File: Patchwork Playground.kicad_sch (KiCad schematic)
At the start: 93 parts, among them J1 PADS, J2 USB_C_Receptacle_USB2.0, J3 PADS, J4 POGO, J5 PADS, J6 JST-GH-4P, SW1 SW_SPDT, SW2 SW_SPDT, SW3 SW_SPDT, SW4 BUTTON, SW5 SW_SPDT, SW6 SW_SPDT, SW7 SW_SPDT, U1 SMF05CT1G, U2 M3406, U3 BQ21040DBVR, U4 SMF05CT1G, U5 QMC5883L, U6 BC805M, U7 LSM6DSV

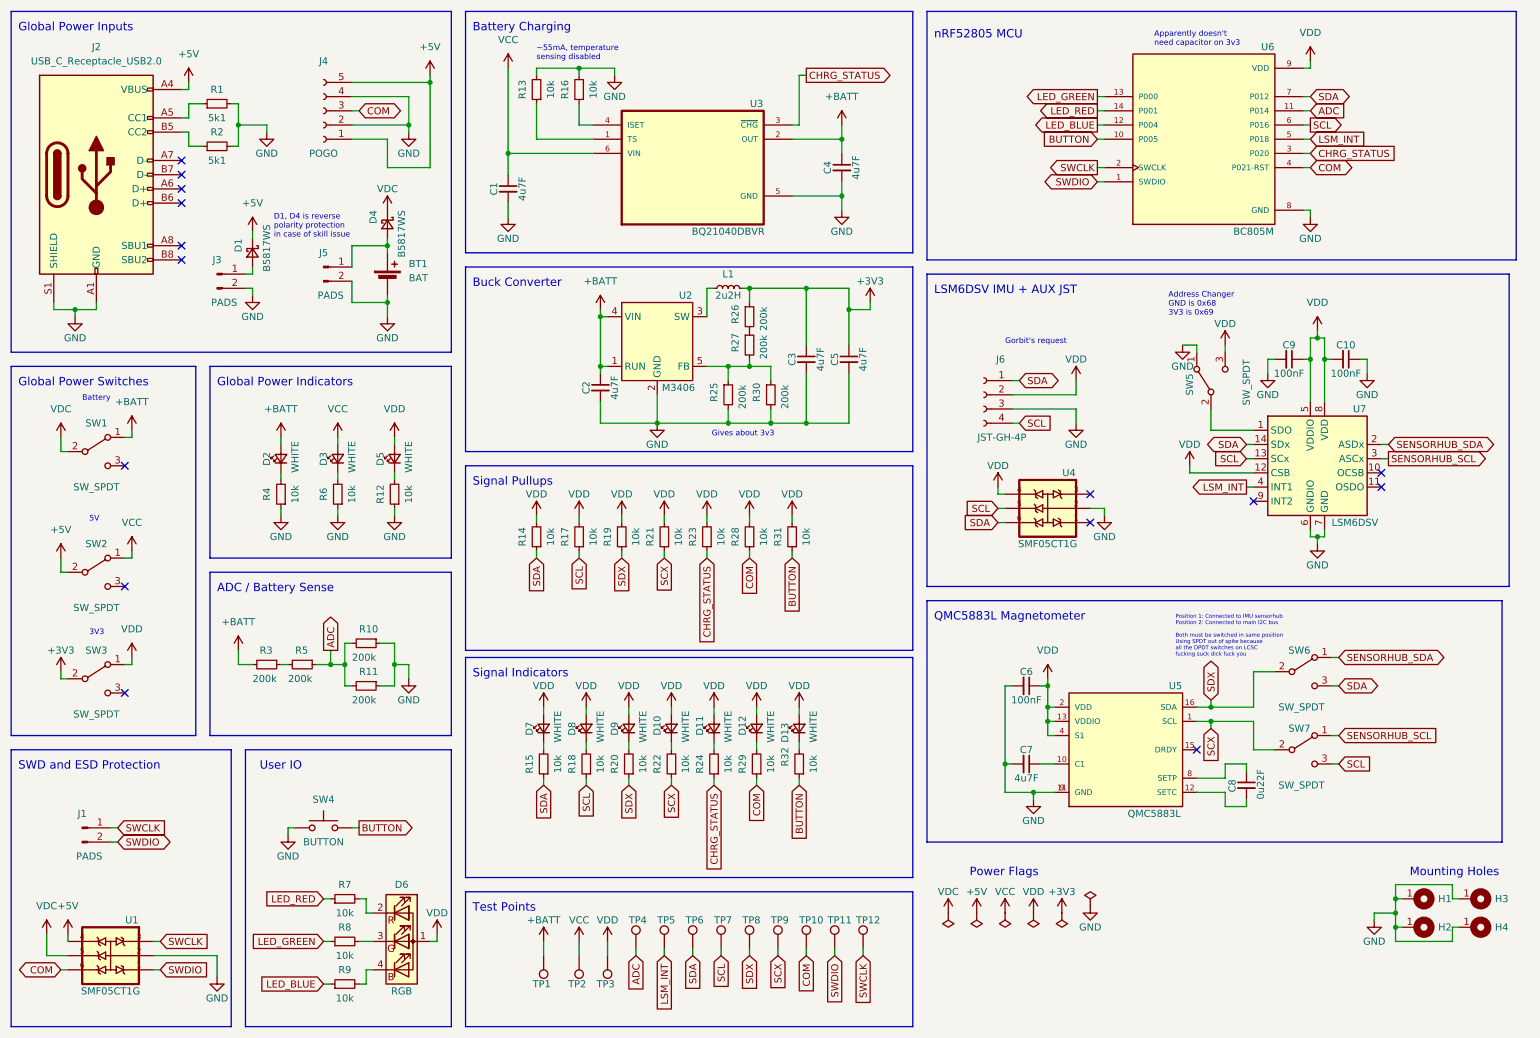
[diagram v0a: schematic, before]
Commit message: change swd footprint
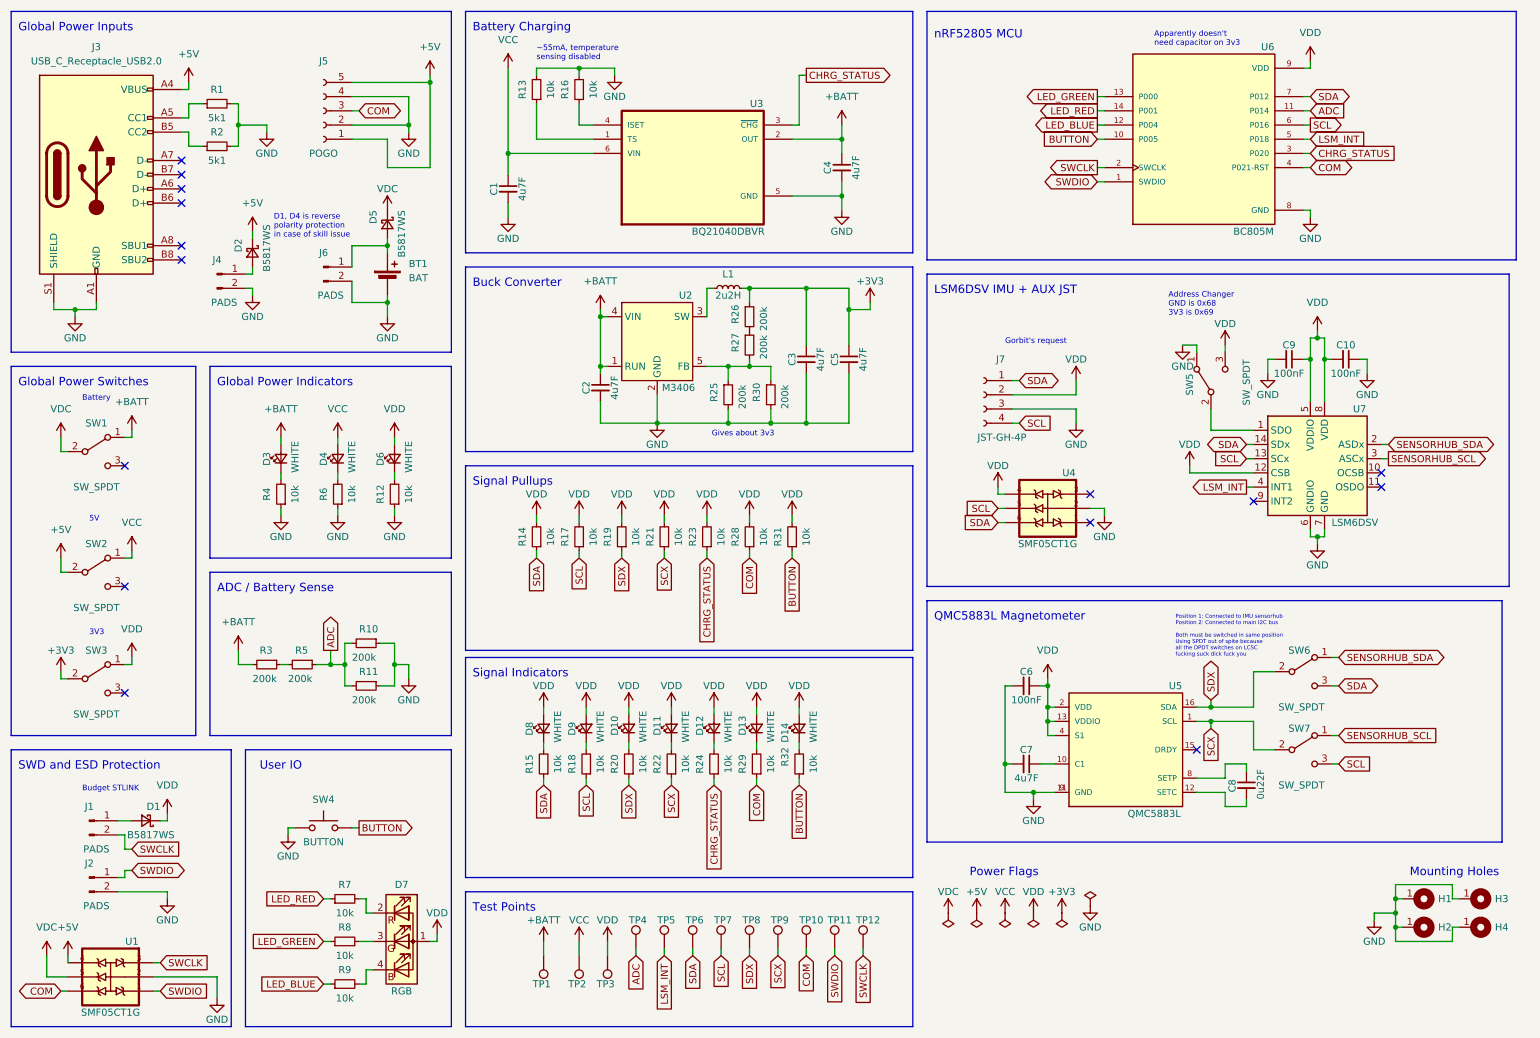
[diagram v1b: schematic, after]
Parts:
- added D1: B5817WS, Patchwork Playground Footprints:D_SOD-323, symbol Patchwork Playground Symbols:D_Schottky_Small
- added J2: PADS, Patchwork Playground Footprints:PinHeader_1x02_P2.54mm_Vertical, symbol Patchwork Playground Symbols:Conn_01x02_Pin
- renumbered D9 to D10, D10 to D11, D11 to D12, D12 to D13, D13 to D14, D1 to D2, D2 to D3, D3 to D4, D4 to D5, D5 to D6, D6 to D7, D7 to D8, D8 to D9, J2 to J3, J3 to J4, J4 to J5, J5 to J6, J6 to J7
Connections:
- net GND: now also J2.2 (Pin_2)
- net SWCLK: now also J1.2 (Pin_2); no longer J1.1 (Pin_1)
- net SWDIO: now also J2.1 (Pin_1); no longer J1.2 (Pin_2)
- net VDD: now also D1.1 (K)
- new net: D1.2 (A), J1.1 (Pin_1)
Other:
- note added: "Budget STLINK"
- moved on the sheet: J1, U1

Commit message: change adc/buck res values, fix qmc sensorhub pullups
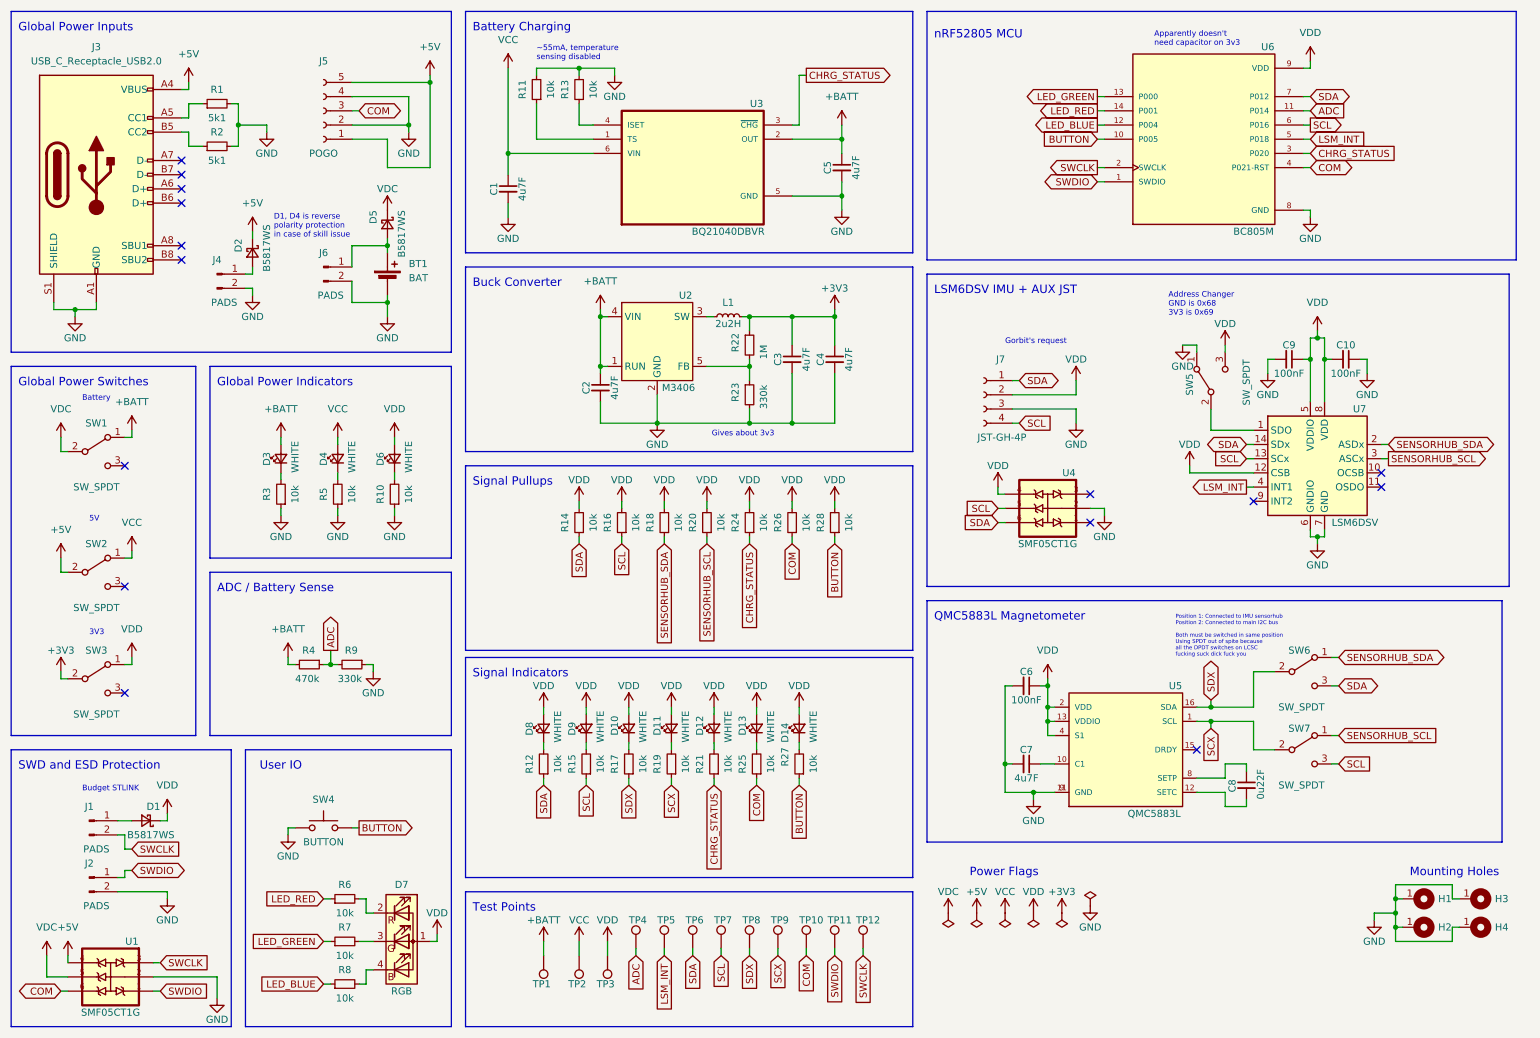
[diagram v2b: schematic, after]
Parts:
- removed R10, R25, R26, R3: 200k, Patchwork Playground Footprints:R_0603_1608Metric, symbol Patchwork Playground Symbols:R_Small
- R22: renamed from R27; value 200k -> 1M
- R23: renamed from R30; value 200k -> 330k
- R4: renamed from R5; value 200k -> 470k
- R9: renamed from R11; value 200k -> 330k
- renumbered C5 to C4, C4 to C5, R12 to R10, R13 to R11, R15 to R12, R16 to R13, R18 to R15, R17 to R16, R20 to R17, R19 to R18, R22 to R19, R21 to R20, R24 to R21, R23 to R24, R29 to R25, R28 to R26, R32 to R27, R31 to R28, R4 to R3, R6 to R5, R7 to R6, R8 to R7, R9 to R8
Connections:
- net +3V3: now also R22.1
- net +BATT: now also R4.2
- net SCX: no longer R20.1
- net SDX: no longer R18.1
- net SENSORHUB_SCL: now also R20.1
- net SENSORHUB_SDA: now also R18.1
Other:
- moved on the sheet: C3, C4, L1, R14, R16, R18, R20, R23, R24, R26, R28, R4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

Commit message: maybe include the actual prod files you big dummy
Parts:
- R22: MPN C25811 -> C22935
- R23, R9: MPN C25811 -> C23137
- R4: MPN C25811 -> C23178
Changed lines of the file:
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@@
       (effects (font (size 1.27 1.27)) hide)
     )
-    (property "MPN" "C25811" (at 74.93 130.81 0)
+    (property "MPN" "C23137" (at 74.93 130.81 0)
       (effects (font (size 1.27 1.27)) hide)
     )
@@
       (effects (font (size 1.27 1.27)) hide)
     )
-    (property "MPN" "C25811" (at 67.31 130.81 0)
+    (property "MPN" "C23178" (at 67.31 130.81 0)
       (effects (font (size 1.27 1.27)) hide)
     )
@@
       (effects (font (size 1.27 1.27)) hide)
     )
-    (property "MPN" "C25811" (at 146.05 73.66 0)
+    (property "MPN" "C22935" (at 146.05 73.66 0)
       (effects (font (size 1.27 1.27)) hide)
     )
@@
       (effects (font (size 1.27 1.27)) hide)
     )
-    (property "MPN" "C25811" (at 146.05 82.55 0)
+    (property "MPN" "C23137" (at 146.05 82.55 0)
       (effects (font (size 1.27 1.27)) hide)
     )

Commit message: fix fix fix fix fix
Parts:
- L1: value 2u2H -> 4u7H; MPN C285966 -> C1034
- R22: value 1M -> 2M; MPN C22935 -> C22976
- R23: value 330k -> 470k; MPN C23137 -> C23178
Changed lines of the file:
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@@
       (effects (font (size 1.27 1.27)))
     )
-    (property "Value" "2u2H" (at 142.24 69.85 90)
+    (property "Value" "4u7H" (at 142.24 69.85 90)
       (effects (font (size 1.27 1.27)))
     )
@@
       (effects (font (size 1.27 1.27)) hide)
     )
-    (property "MPN" "C285966" (at 142.24 68.58 0)
+    (property "MPN" "C1034" (at 142.24 68.58 0)
       (effects (font (size 1.27 1.27)) hide)
     )
@@
       (effects (font (size 1.27 1.27)) (justify left))
     )
-    (property "Value" "1M" (at 148.59 76.2 90)
+    (property "Value" "2M" (at 148.59 76.2 90)
       (effects (font (size 1.27 1.27)) (justify left))
     )
@@
       (effects (font (size 1.27 1.27)) hide)
     )
-    (property "MPN" "C22935" (at 146.05 73.66 0)
+    (property "MPN" "C22976" (at 146.05 73.66 0)
       (effects (font (size 1.27 1.27)) hide)
     )
@@
       (effects (font (size 1.27 1.27)) (justify left))
     )
-    (property "Value" "330k" (at 148.59 85.09 90)
+    (property "Value" "470k" (at 148.59 85.09 90)
       (effects (font (size 1.27 1.27)) (justify left))
     )
@@
       (effects (font (size 1.27 1.27)) hide)
     )
-    (property "MPN" "C23137" (at 146.05 82.55 0)
-      (effects (font (size 1.27 1.27)) hide)
-    )
+    (property "MPN" "C23178" (at 146.05 82.55 0)
+      (effects (font (size 1.27 1.27)) hide)
+    )

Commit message: v1.1
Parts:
- removed D5: B5817WS, Patchwork Playground Footprints:D_SOD-323, symbol Patchwork Playground Symbols:D_Schottky_Small
- removed D7: RGB, Patchwork Playground Footprints:LED_RGB_1210, symbol Patchwork Playground Symbols:LED_ARGB
- removed J1, J2: PADS, Patchwork Playground Footprints:PinHeader_1x02_P2.54mm_Vertical, symbol Patchwork Playground Symbols:Conn_01x02_Pin
- removed R14, R16, R24, R26, R28: 10k, Patchwork Playground Footprints:R_0603_1608Metric, symbol Patchwork Playground Symbols:R_Small
- added C1: 100nF, Patchwork Playground Footprints:C_0603_1608Metric, symbol Patchwork Playground Symbols:C_Small
- added D6: RGB, Patchwork Playground Footprints:LED_RGB_1210, symbol Patchwork Playground Symbols:LED_RGAB
- added J1: SWD_HEADER, Patchwork Playground Footprints:PinHeader_1x04_P2.54mm_Vertical, symbol Patchwork Playground Symbols:Conn_01x04_Socket
- added SW4: BUTTON, Patchwork Playground Footprints:SW_Push_1P1T_XKB_TS-1187A, symbol Patchwork Playground Symbols:SW_Push
- BT1, H1, H2, H3, H4, TP1, TP10, TP11, TP12, TP2, TP3, TP4, TP5, TP6, TP7, TP8, TP9: MPN (none) -> N/A
- C2: renamed from C1; value 4u7F -> 4.7uF
- C3: renamed from C2; value 4u7F -> 4.7uF
- C4: renamed from C3; value 4u7F -> 4.7uF
- C5: renamed from C4; value 4u7F -> 4.7uF
- C6: renamed from C5; value 4u7F -> 4.7uF
- C8: renamed from C7; value 4u7F -> 4.7uF
- C9: renamed from C8; value 0u22F -> 220nF
- D1, D2, SW1, SW2, SW3, U2, U7: EXTENDED? YES -> (none)
- J3: renamed from J4; MPN (none) -> N/A
- J4: renamed from J5; MPN (none) -> N/A
- J5: renamed from J6; MPN (none) -> N/A
- J6: renamed from J7; symbol Connector:Conn_01x04_Socket -> Patchwork Playground Symbols:Conn_01x04_Socket; MPN (none) -> C189895
- L1: value 4u7H -> 4.7uH; EXTENDED? YES -> (none)
- SW6: renamed from SW5; EXTENDED? YES -> (none)
- SW7: renamed from SW6; EXTENDED? YES -> (none)
- SW8: renamed from SW7; EXTENDED? YES -> (none)
- U1, U4: Availability In Stock -> (none); Check_prices https://www.snapeda.com/parts/SMF05CT1G/Onsemi/view-part/?r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 -> (none); DESCRIPTION SMF05C Series 7.2 V 100 W 5-Line Transient Voltage Suppress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 -> (none); MANUFACTURER ON Semiconductor -> (none); MF onsemi -> (none); MP SMF05CT1G -> (none); PACKAGE SOT-363 ON Semiconductor -> (none); PRICE None -> (none); Package SC-88-6 ON Semiconductor -> (none); Price None -> (none); Purchase-URL https://www.snapeda.com/api/url_track_click_mouser/?unipart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 -> (none); STANDARD IPC7351B -> (none); SnapEDA_Link https://www.snapeda.com/parts/SMF05CT1G/Onsemi/view-part/?r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 -> (none)
- U3: Availability In Stock -> (none); Check_prices https://www.snapeda.com/parts/BQ21040DBVR/Texas+Instruments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 -> (none); EXTENDED? YES -> (none); MF Texas Instruments -> (none); MP BQ21040DBVR -> (none); Package SOT-23-6 Texas Instruments -> (none); Price None -> (none); Purchase-URL https://www.snapeda.com/api/url_track_click_mouser/?unipart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 -> (none); SnapEDA_Link https://www.snapeda.com/parts/BQ21040DBVR/Texas+Instruments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 -> (none)
- U5: Availability In Stock -> (none); Check_prices https://www.snapeda.com/parts/HMC5883L-T/Honeywell+Aerospac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 -> (none); EXTENDED? YES -> (none); MF Honeywell Aerospace -> (none); MP HMC5883L-T -> (none); Package LCC-16 Honeywell -> (none); Price None -> (none); Purchase-URL https://www.snapeda.com/api/url_track_click_mouser/?unipart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 -> (none); SnapEDA_Link https://www.snapeda.com/parts/HMC5883L-T/Honeywell+Aerospac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 -> (none)
- U6: Availability In Stock -> (none); Check_prices https://www.snapeda.com/parts/BC805M/Fanstel+Corp./view-par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 -> (none); MANUFACTURER Fanstel Corporation -> (none); MAXIMUM_PACKAGE_HEIGHT 1.9mm -> (none); MF Fanstel Corp. -> (none); MP BC805M -> (none); MPN (none) -> C6751361; PARTREV 1.03 -> (none); Package SMD-14 Fanstel Corp. -> (none); Price None -> (none); Purchase-URL https://www.snapeda.com/api/url_track_click_mouser/?unipart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 -> (none); SNAPEDA_PN BC805M -> (none); STANDARD Manufacturer Recommendations -> (none); SnapEDA_Link https://www.snapeda.com/parts/BC805M/Fanstel+Corp./view-par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 -> (none); now in the parts list
- renumbered C9 to C10, C10 to C11, C6 to C7, D11 to D10, D12 to D11, D13 to D12, D14 to D13, D6 to D5, D8 to D7, D9 to D8, D10 to D9, J3 to J2, R15 to R14, R17 to R15, R19 to R16, R22 to R17, R23 to R18, R21 to R19, R25 to R20, R27 to R21, R18 to R22, R20 to R23, SW4 to SW5
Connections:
- net ADC: now also U6.10 (P005), C1.2; no longer U6.11 (P014)
- net GND: now also C1.1, J1.4 (Pin_4), SW4.1
- net LED_BLUE: now also U6.11 (P014); no longer U6.12 (P004)
- net LED_GREEN: now also U6.12 (P004); no longer U6.13 (P000)
- net LED_RED: now also U6.13 (P000); no longer U6.14 (P001)
- net SCL: now also U6.5 (P018); no longer U6.6 (P016)
- net SDA: now also U6.6 (P016); no longer U6.7 (P012)
- net SWCLK: now also J1.2 (Pin_2)
- net SWDIO: now also J1.3 (Pin_3)
- net VDC: now also BT1.1 (+), J5.1 (Pin_1)
- net VDD: now also D6.3 (A)
- net at R6.2: now also D6.1 (RK)
- net at R7.2: now also D6.2 (GK)
- net at R8.2: now also D6.4 (BK)
- net at D1.2 (A): now also J1.1 (Pin_1)
- net BUTTON renamed BTN
- net BTN: now also U6.14 (P001); no longer U6.10 (P005)
- net CHRG_STATUS renamed CHRG
- net COM renamed DOCK
- net DOCK: now also SW4.2
- net LSM_INT renamed INT
- net INT: now also U6.7 (P012); no longer U6.5 (P018)
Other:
- note added: "Doesn't need cap on VDD Has internal pull-ups/pull-downs Only pins 004 and 005 are ADC"
- note added: "Position 1: Connected to IMU sensorhub Position 2: Connected to main I2C bus Both must be switched in same position Using SPDT out of spite because all the DPDT switches on LCSC fucking suck shit fuck you"
- note added: "x2.42(42) Adding 100nF reduces noise apparently?"
- note removed: "Apparently doesn't need capacitor on 3v3"
- note removed: "Budget STLINK"
- note removed: "D1, D4 is reverse polarity protection in case of skill issue"
- note removed: "Position 1: Connected to IMU sensorhub Position 2: Connected to main I2C bus Both must be switched in same position Using SPDT out of spite because all the DPDT switches on LCSC fucking suck dick fuck you"
- note removed: "Signal Pullups"
- moved on the sheet: BT1, C2, C3, C4, C5, C6, C7, C8, C9, D10, D11, D12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
